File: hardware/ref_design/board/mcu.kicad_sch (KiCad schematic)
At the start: 8 parts, among them U4 RP2354B, X1 12MHz

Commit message: Reference design: checklist changes and the datasheet pin gate
Board: PWR_HOLD pull-down (R42, also covers RP2350-E9), charge current
3.3k (333-364 mA), firmware charge pause (CHG_OFF, Q4), R13 33k, 0.1 ohm
in D5's path, JP1/JP2 cut-jumpers, TP6-8, spare 1206 footprints, 4-bit
revision strap on GPIO22-25 (REV 1 on the back).

Datasheet review of every part's pins (pin_review/, tools/check_pins.py)
found and fixed: J6 TX/RX swapped against Raspberry Pi's debug connector
spec, USB series resistors 22 to 27 ohm, the ME6211 CE able to lead its
VIN at a live plug-in (C47 on PWR_EN).

Case: silicone height 1.2 mm from the DS Lite, chamfered step.

Co-Authored-By: Claude Opus 5.5 <noreply@anthropic.com>
Claude-Session: https://claude.ai/code/session_01MUt6paNsT75sqwAr83zRS3
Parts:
- added R48: DNP, Resistor_SMD:R_0402_1005Metric, symbol Device:R
- added R49, R50, R51: 1k, Resistor_SMD:R_0402_1005Metric, symbol Device:R
- R21, R22: value 22 -> 27; LCSC C25092 -> C25100; MPN 0402WGF220JTCE -> 0402WGF270JTCE
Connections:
- net GND: now also R48.2, R49.2, R50.2, R51.2
- net CHG_OFF: now reaches U4.19 (GPIO19)
- net REV0: now reaches U4.22 (GPIO22)
- net REV0: now also R48.1
- net REV1: now reaches U4.23 (GPIO23)
- net REV1: now also R49.1
- net REV2: now reaches U4.25 (GPIO24)
- net REV2: now also R50.1
- net REV3: now reaches U4.26 (GPIO25)
- net REV3: now also R51.1
- no-connect marks 19 -> 14

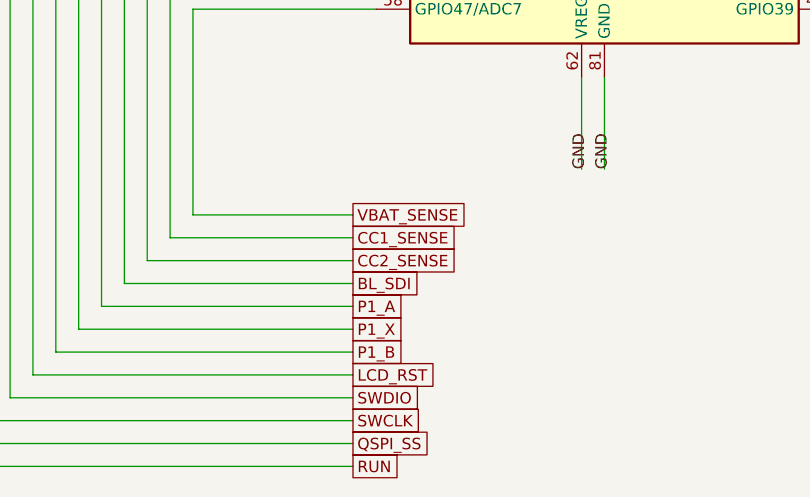
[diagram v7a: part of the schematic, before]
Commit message: Reference design: discrete backlight current sinks replace the AP3156
The AP3156 charge pump (U6, C443652) is out of stock at JLC and LCSC. Each
of the panel's two cathode pins now has its own linear current sink: half
of an MCP6002 (U6, C7377 Preferred) drives an AO3400A (Q5/Q6, C20917 Basic)
and holds a 2.2 ohm sense resistor (R52/R53) at BL_REF. LED_A is on VSYS
through JP2. GPIO44 (now BL_PWM, PWM10 A) sets BL_REF through 100k/3.9k
and 1 uF: 0.124 V at 100% = 56 mA a pin, 113 mA in all (panel max 120).
RG 330 ohm, RF 10k, CF 1 nF, gate pull-downs 100k: simulated first
(board/sim, previous commit), phase margin >= 72.5 deg at every corner.

Every new part is Basic or Preferred: 12 extended part numbers instead of
13, parts $4.77 a board instead of $5.01, about $16.81 a unit at 10.

Layout: the sinks sit above J3's LED pins between J3 and J2, clear of the
ground bar route.py lays over J3's grounded pins; board rebuilt and
re-routed (route.py, 80 passes): DRC 0 errors, 0 unconnected, 0 parity,
2 cosmetic warnings as before. check_netlist, check_pins (29 parts, 244
pins, 94 passives), ERC 0, check_fit pass. silk.py puts J2's BATT label
above it (the op-amp is now on its left).

Docs: pin reviews for U6 and Q5/Q6 with page cites, passives, U4 (GPIO44)
and the panel; pinmap (GPIO44 PWM, backlight section), bring-up step 5,
design review, PLAN (also: the USB series resistors are 27 ohm, not 22),
BOM, assembly, validation plan items, SOURCES.

Co-Authored-By: Claude Opus 5.5 <noreply@anthropic.com>
Claude-Session: https://claude.ai/code/session_01Ceq1EsbekLwXHokcQ73Ldk
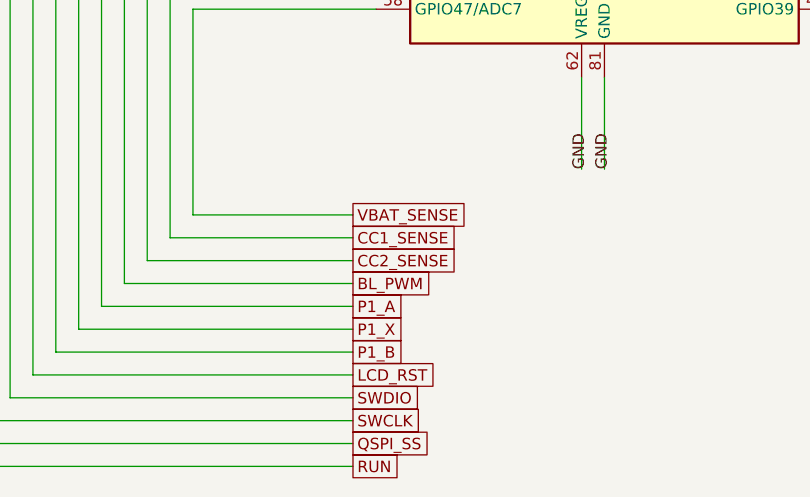
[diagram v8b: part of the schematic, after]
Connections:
- net BL_SDI renamed BL_PWM
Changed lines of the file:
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@@
     (at 58.42 175.26 0)
 )
-  (global_label "BL_SDI"
+  (global_label "BL_PWM"
     (shape passive)
     (at 58.42 172.72 0)
